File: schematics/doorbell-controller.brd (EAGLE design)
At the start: 114.3 x 100 mm, 11 parts, among them Q1 BC557

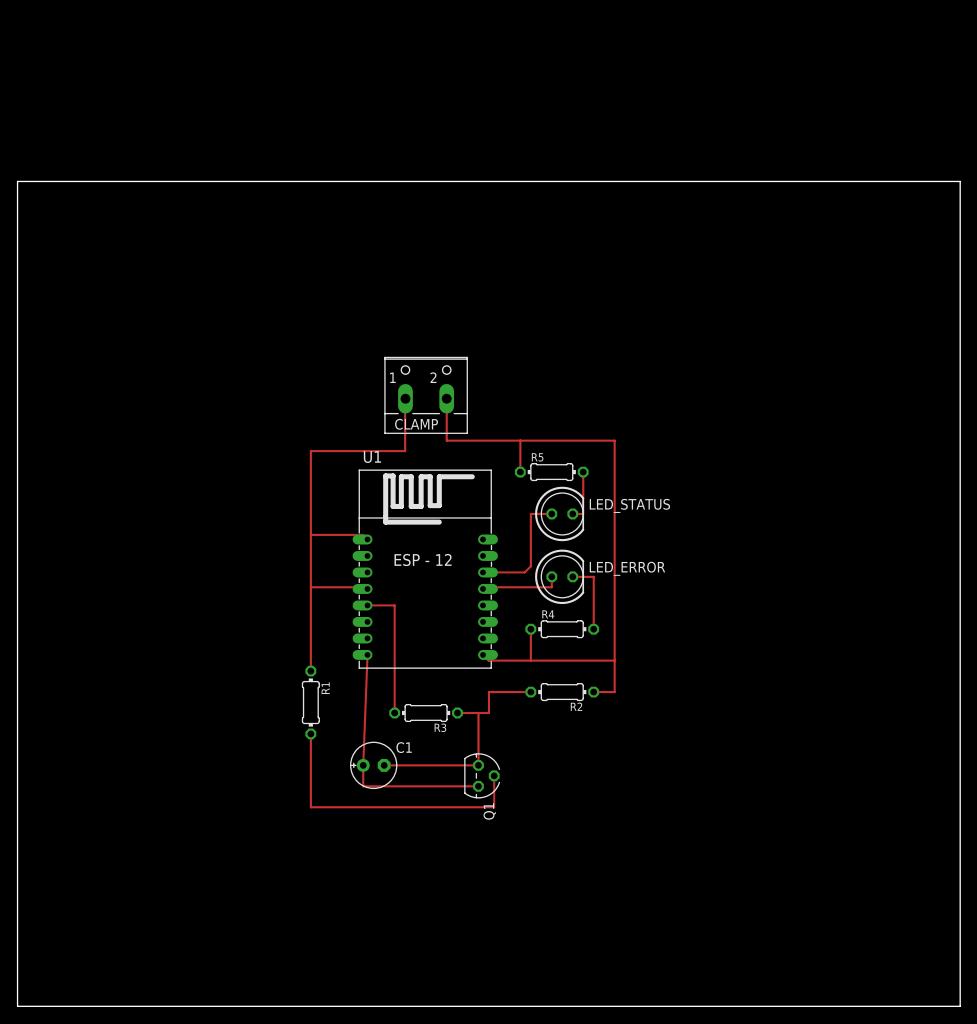
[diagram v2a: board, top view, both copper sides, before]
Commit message: Updated Schematics to fit wall mount dimensions
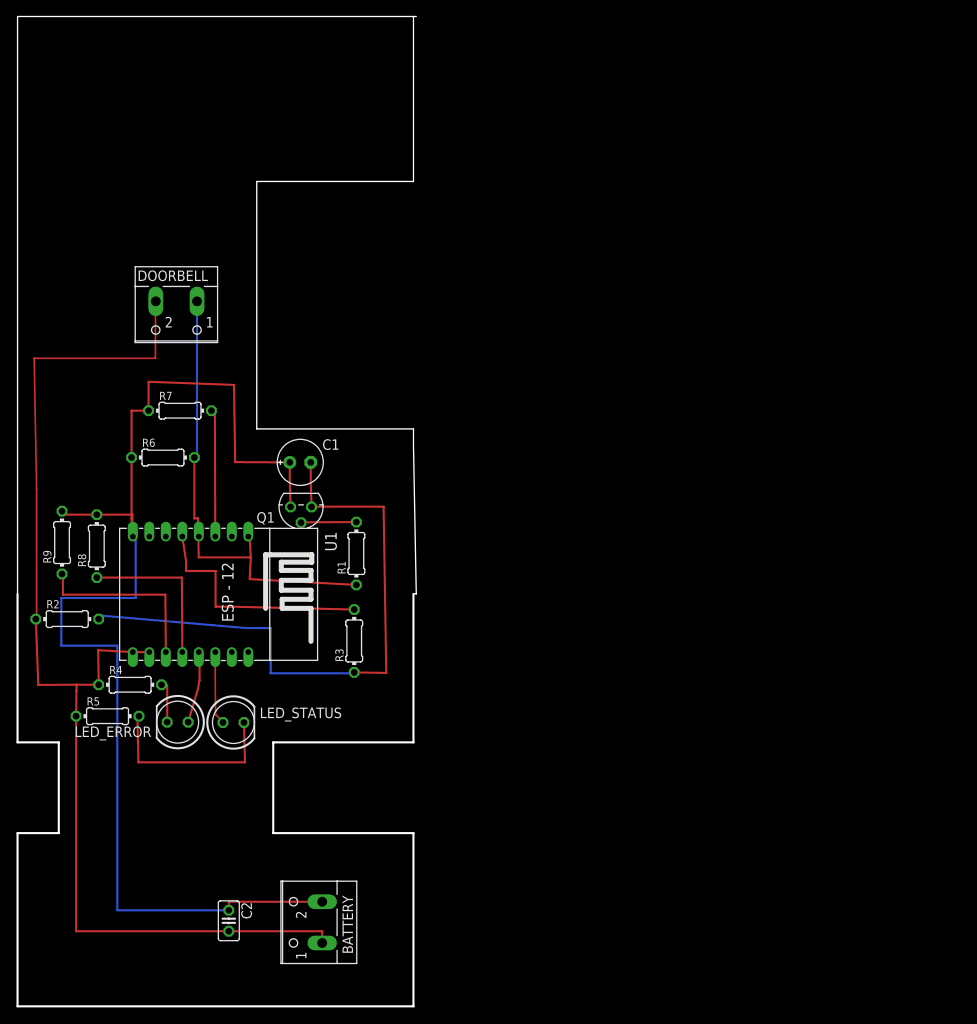
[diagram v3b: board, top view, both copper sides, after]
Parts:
- removed CLAMP: (no value), con-wago-500:W237-102
- added BATTERY, DOORBELL: (no value), con-wago-500:W237-102
- added C2: 0.1uF, rcl:C025-025X050
- added R6, R7, R8: 10k, rcl:0204/7
- added R9: 330, rcl:0204/7
- C1: value 100u -> 100uF
- moved R5 61.5 mm to (10.9, 35.2)
- moved R2 60.7 mm to (6.03, 46.9), turned to 0 degrees
- moved R4 52.8 mm to (13.6, 39.0)
- moved LED_ERROR 49.8 mm to (19.4, 34.5), turned to 180 degrees
- moved LED_STATUS 47.2 mm to (26.2, 34.4)
- moved Q1 39.1 mm to (34.4, 60.5), turned to 180 degrees
- moved C1 37.8 mm to (34.3, 65.9)
- moved U1 27.4 mm to (22.2, 49.8), turned to 270 degrees
- moved R1 18.9 mm to (41.1, 54.9), turned to 90 degrees
- moved R3 12.3 mm to (40.8, 44.3), turned to 90 degrees
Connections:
- new net N$10: R7.2, U1.EN
- new net N$11: R8.1, U1.GPIO0
- new net N$9: R9.1, U1.GPIO2
- net GND: now also BATTERY.1, C2.2, DOORBELL.2, U1.GPIO15; no longer CLAMP.2
- net N$8: now also BATTERY.2, C2.1, R6.1, R7.1, R8.2, R9.2
- net RST: now also DOORBELL.1, R6.2; no longer CLAMP.1
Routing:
- net N$8: track 29.9 -> 151.5 mm
- net GND: track 82.3 -> 140.3 mm
- net N$5: track 29.2 -> 75.3 mm
- net N$2: track 34.9 -> 6.71 mm
- net N$9: track 0.00 -> 22.0 mm
- net N$11: track 0.00 -> 19.3 mm
- net N$7: track 6.35 -> 23.5 mm
- net N$10: track 0.00 -> 15.7 mm
- net N$3: track 16.3 -> 28.9 mm
- net N$1: track 15.0 -> 8.91 mm
- net N$6: track 8.89 -> 5.22 mm
- net N$4: track 9.69 -> 8.91 mm
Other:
- board size 114.3 x 100 mm -> 48.3 x 120 mm

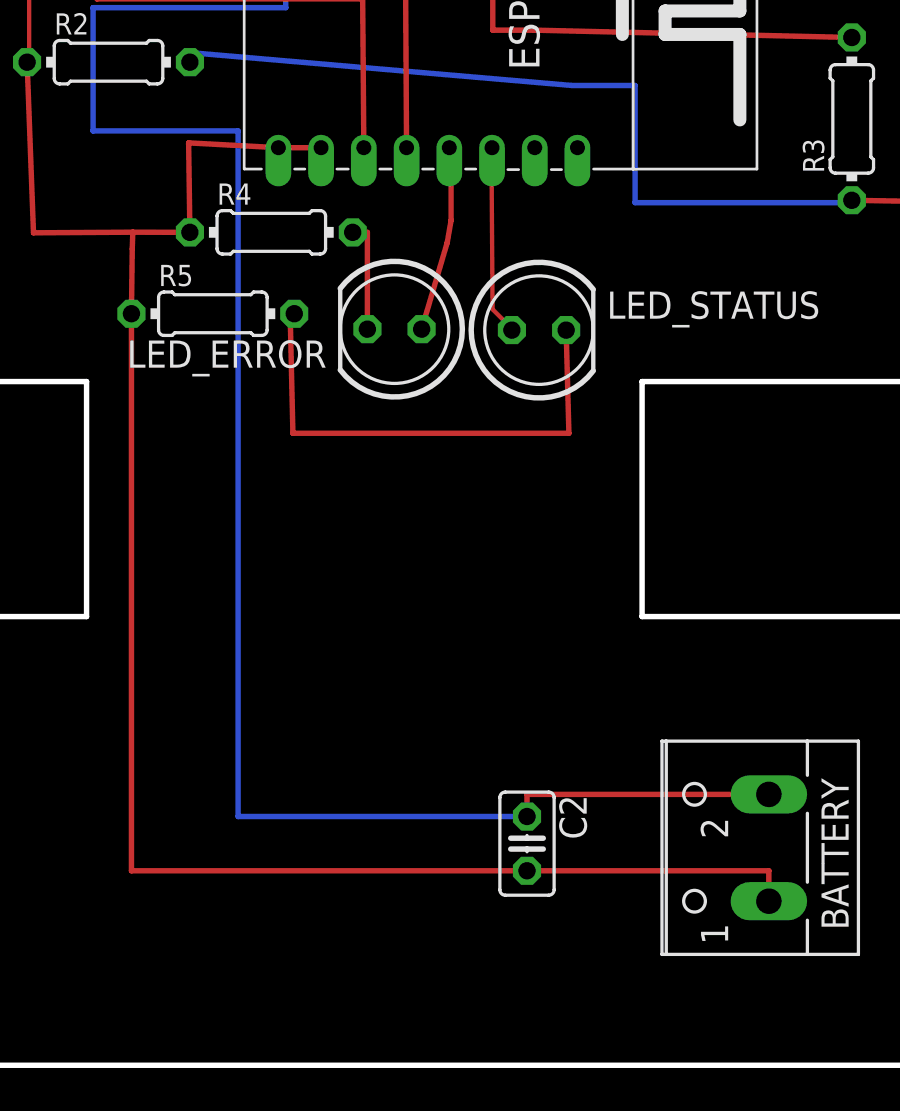
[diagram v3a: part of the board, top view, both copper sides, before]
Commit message: Added voltage regulator to schematics
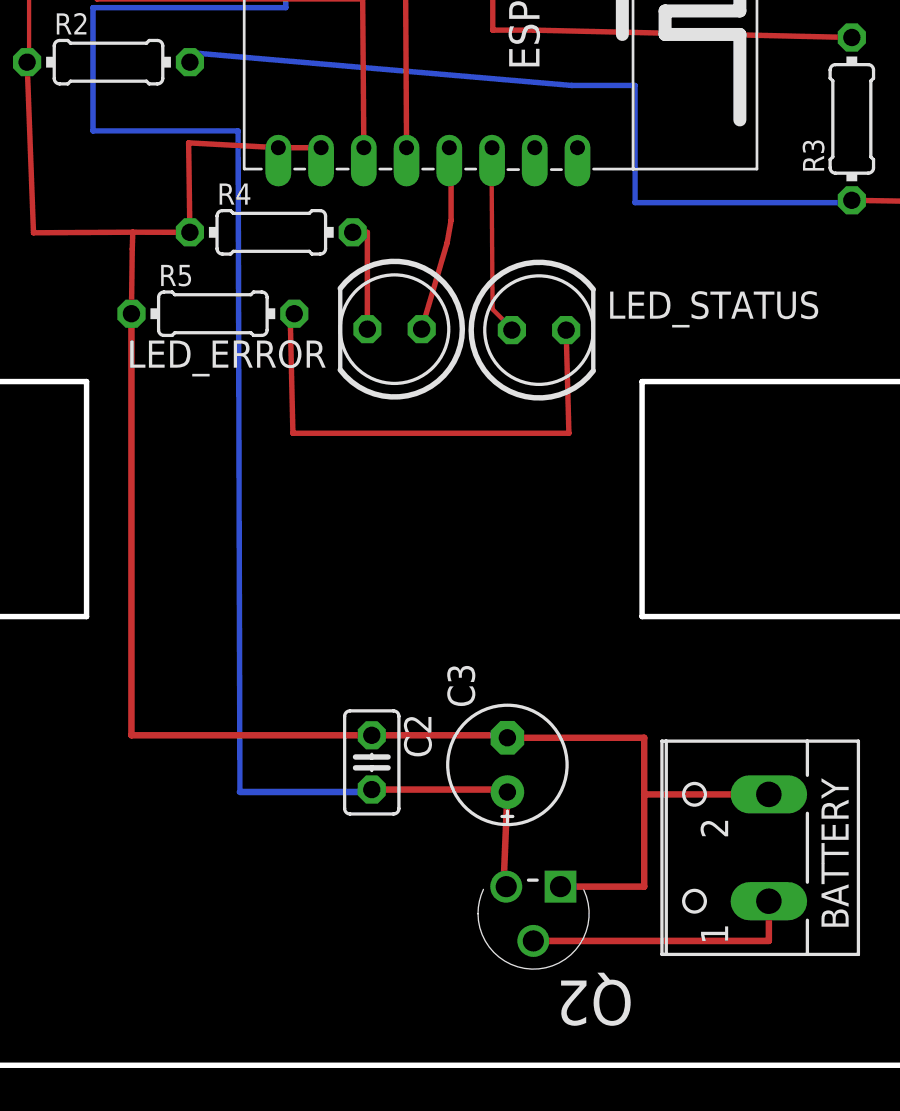
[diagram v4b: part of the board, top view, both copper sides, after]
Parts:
- added C3: 100uF, rcl:E2,5-6E
- added Q2: MCP1702-3302E/TO, Microchip_By_element14_Batch_1:TO127P254X533-3
- moved C2 8.20 mm to (18.3, 14.2)
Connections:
- removed net N$8: BATTERY.2, C1.+, C2.1, Q1.1, R6.1, R7.1, R8.2, R9.2, U1.VCC
- new net BATT_VIN: BATTERY.1, Q2.2
- new net VCC: C1.+, C2.2, C3.+, Q1.1, Q2.3, R6.1, R7.1, R8.2, R9.2, U1.VCC
- net GND: now also BATTERY.2, C2.1, C3.-, Q2.1; no longer BATTERY.1, C2.2
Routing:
- net N$8: track 151.5 -> 0.00 mm
- net VCC: track 0.00 -> 141.8 mm
- net BATT_VIN: track 0.00 -> 12.9 mm
- net GND: track 140.3 -> 143.5 mm
